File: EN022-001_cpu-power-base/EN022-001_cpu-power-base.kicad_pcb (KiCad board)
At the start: 2 copper layers, 100 x 100 mm, 31 parts, among them J1 MEGA BOTTOM, J10 GBA_Slot, J3 CART SLOT TOP ROW, J4 CART SLOT FRONT ROW, J6 5V USB, J7 Conn_01x07, J8 EXP2, J9 EXP1, M2_1 Screw_Terminal_01x01, M2_2 Screw_Terminal_01x01, M2_3 Screw_Terminal_01x01, M2_4 Screw_Terminal_01x01, M2_5 Screw_Terminal_01x01, M2_6 Screw_Terminal_01x01, M2_7 Screw_Terminal_01x01, M2_8 Screw_Terminal_01x01, M2_9 Screw_Terminal_01x01, SW1 VOLTAGE, SW2 POWER, U1 TPS2113PW, U2 DS3231MZ

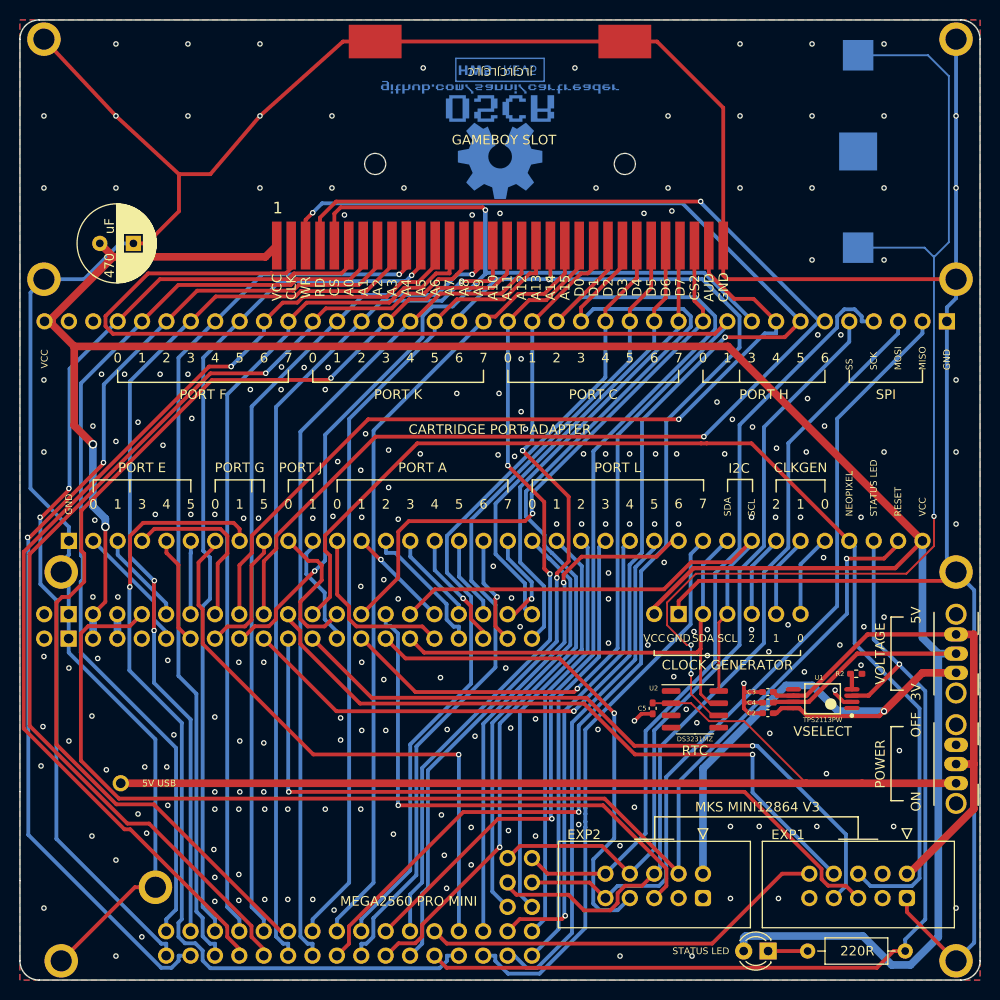
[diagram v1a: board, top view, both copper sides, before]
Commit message: mountin holes position
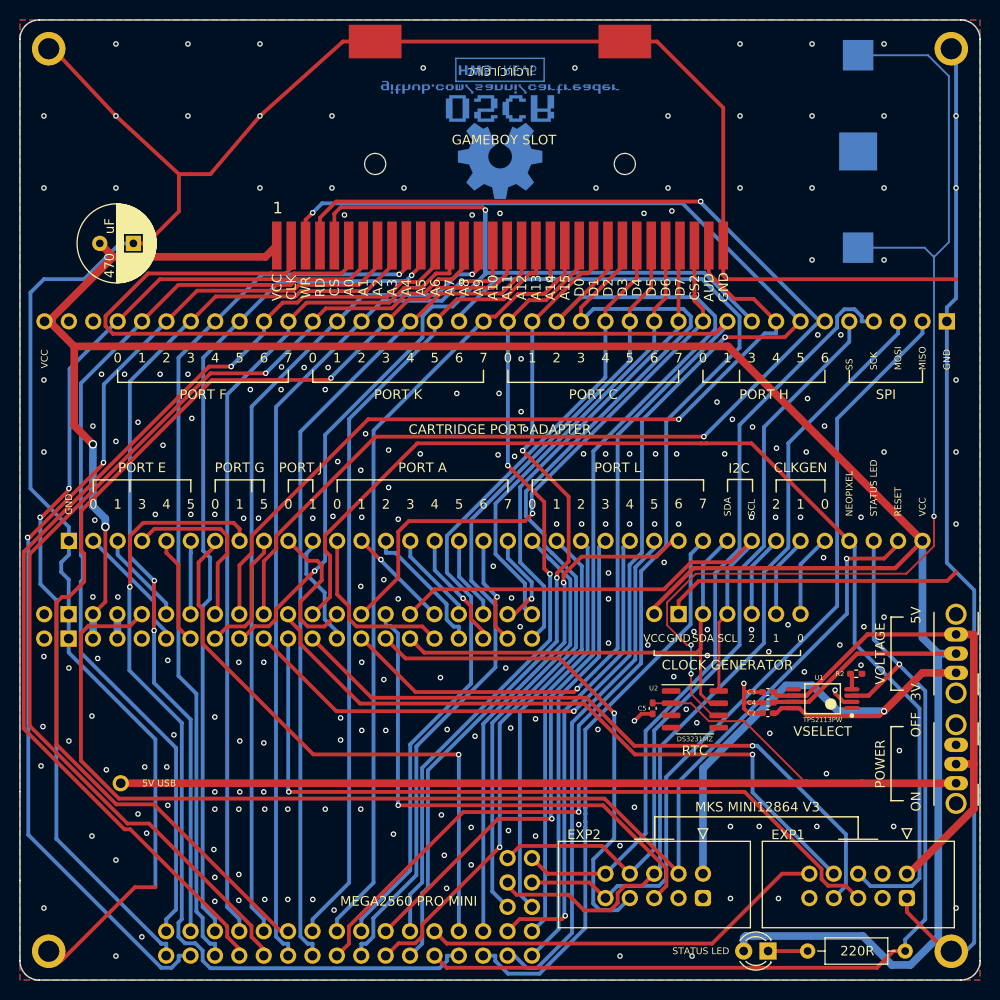
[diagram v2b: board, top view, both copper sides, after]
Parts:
- removed M2_5, M2_6, M2_7, M2_8, M2_9: Screw_Terminal_01x01, MountingHole:MountingHole_2.2mm_M2_ISO7380_Pad
- moved M2_3 117.6 mm to (103.0, 147.0)
- moved M2_4 39.5 mm to (197.0, 147.0)
- moved M2_1 1.12 mm to (103.0, 53.0)
- moved M2_2 1.12 mm to (197.0, 53.0)

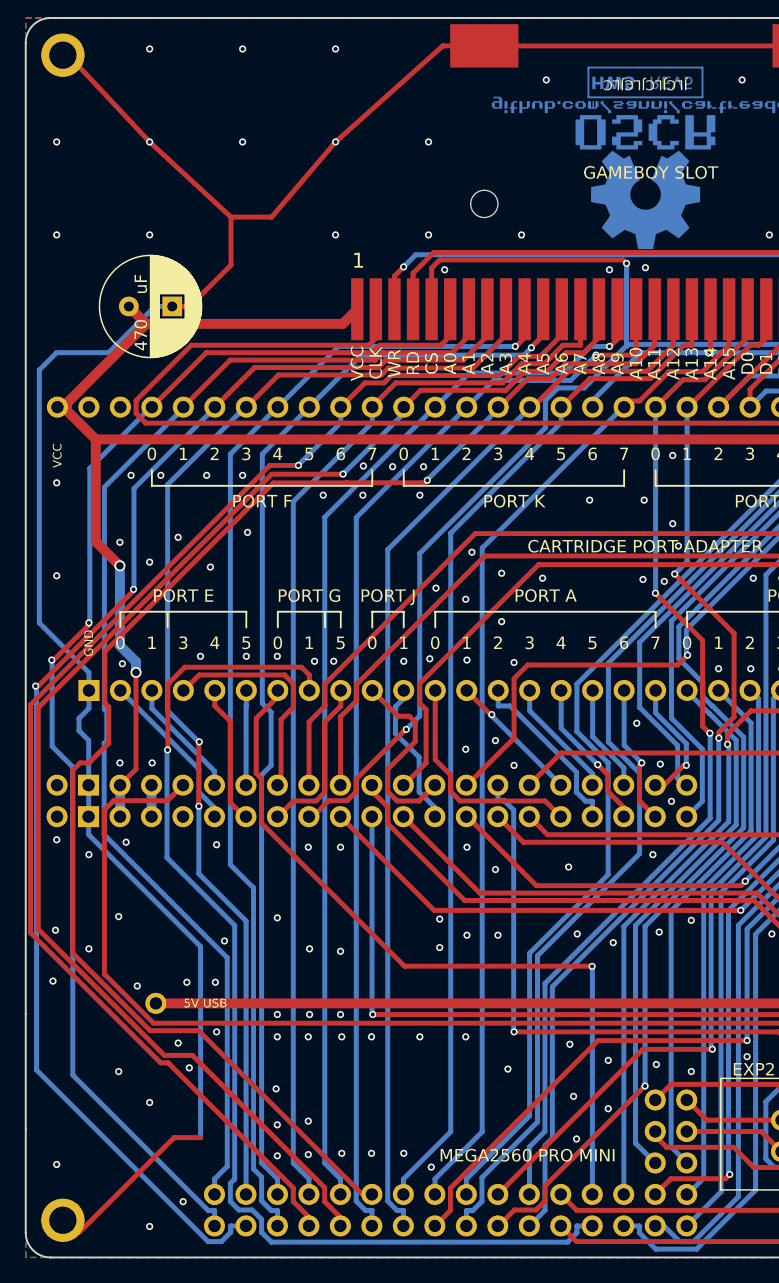
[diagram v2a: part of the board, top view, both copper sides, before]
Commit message: Removed atmega board connector
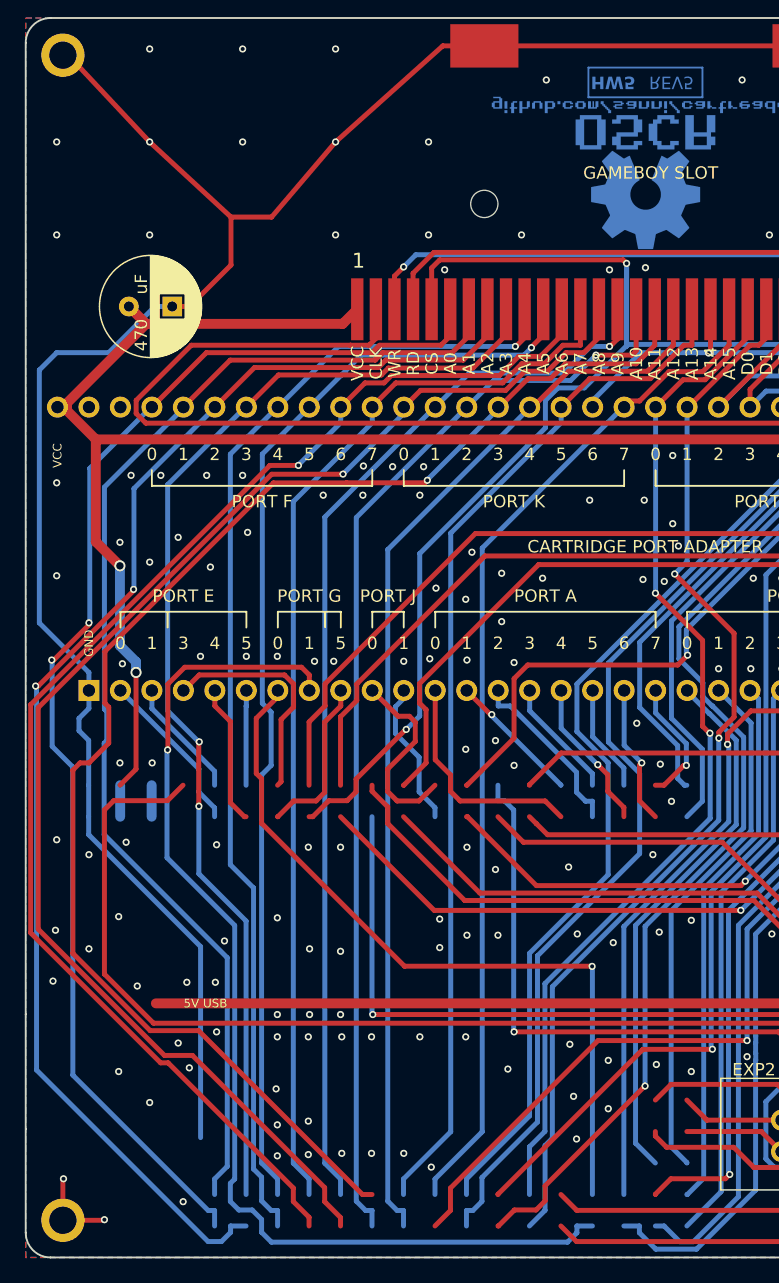
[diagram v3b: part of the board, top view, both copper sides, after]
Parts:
- removed J1: MEGA BOTTOM, !OSCR:MEGA2560_PRO_MINI
- removed J6: 5V USB, Connector_PinHeader_2.54mm:PinHeader_1x01_P2.54mm_Vertical
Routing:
- net GND: track 382.8 -> 376.5 mm
- net +3.3VA: track 2.54 -> 0.00 mm
- net (no net): track 0.00 -> 2.54 mm
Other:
- board text removed: "JLCJLCJLCJLC"

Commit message: updateted GBA slot
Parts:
- added U3: CH32V307VCT6, Package_QFP:LQFP-100_14x14mm_P0.5mm, F.Cu at (147.3, 122.8)
- added U7: AMS1117-3.3, Package_TO_SOT_SMD:SOT-223-3_TabPin2, F.Cu at (108.6, 139.3)
- J10: footprint !sanni:GBA-SLOT-B -> !OSCR:GBA_Slot
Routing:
- net A12: track 88.2 -> 86.9 mm, vias 0 -> 1
- net GND: vias 215 -> 212
- net D41: vias 1 -> 2
- net D39: vias 0 -> 1
- net D38: vias 1 -> 2
- net D35: vias 1 -> 2
- net D34: vias 1 -> 2
- net D33: vias 0 -> 1
- net D32: vias 0 -> 1
- net A9: vias 1 -> 2
- net A8: vias 1 -> 2
- net A7: vias 0 -> 1
- net A5: vias 1 -> 2
- net A4: vias 1 -> 2
- net A3: vias 2 -> 3
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
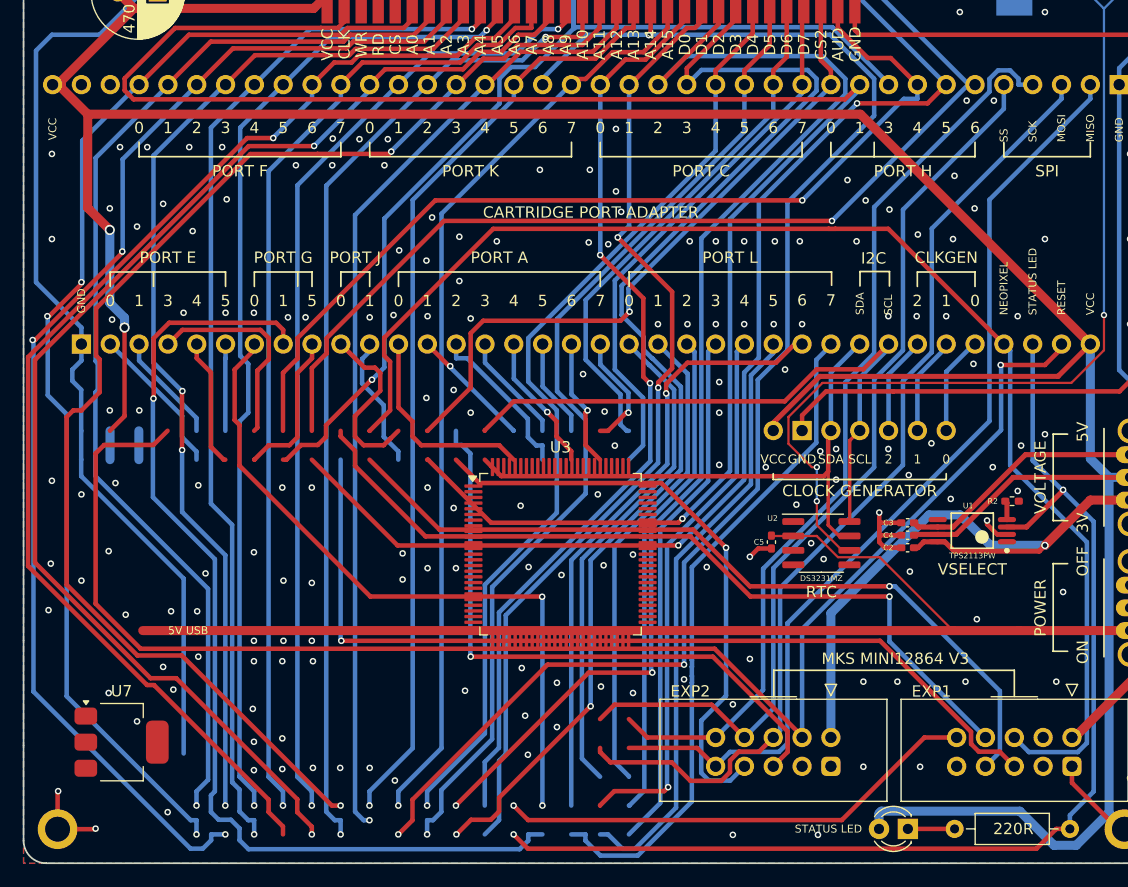
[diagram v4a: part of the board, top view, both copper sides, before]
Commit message: pcb traces cleanup
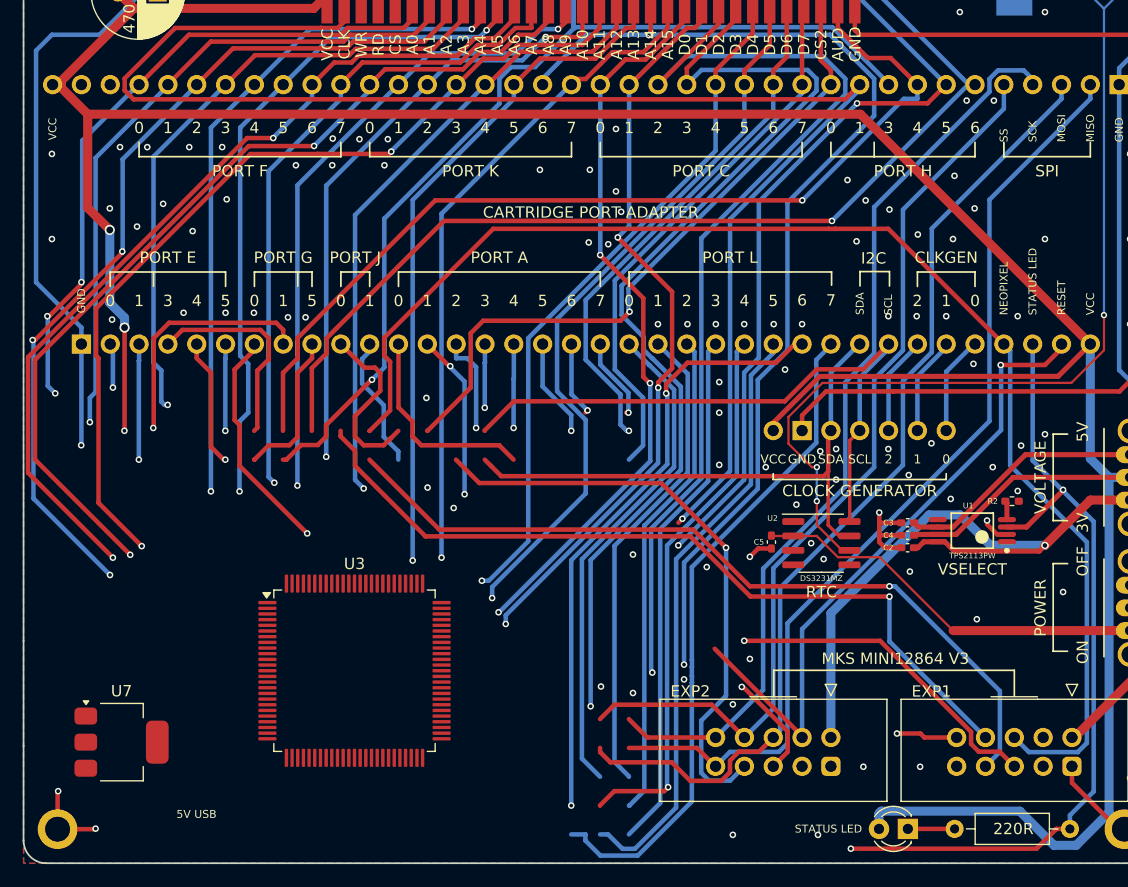
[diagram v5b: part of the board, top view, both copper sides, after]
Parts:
- moved U3 20.9 mm to (129.2, 133.0)
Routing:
- net RESET: track 134.1 -> 57.5 mm
- net VBUS: track 106.5 -> 35.1 mm
- net D40: track 89.7 -> 21.4 mm
- net D10: track 80.5 -> 29.0 mm
- net D19: track 55.0 -> 9.26 mm
- net A0: track 103.9 -> 59.6 mm
- net D41: track 61.5 -> 20.1 mm, vias 2 -> 1
- net A1: track 98.4 -> 60.2 mm
- net A3: track 94.3 -> 57.0 mm, vias 3 -> 1
- net D39: track 42.6 -> 5.40 mm
- net A11: track 115.9 -> 80.2 mm
- net D8: track 149.5 -> 114.1 mm
- net A10: track 89.5 -> 55.4 mm
- net A8: track 113.4 -> 80.8 mm
- net A14: track 127.6 -> 95.1 mm, vias 3 -> 2
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
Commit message: first cimplete  version of CPU POWER BASE
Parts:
- removed BT1: CR1616, !OSCR:CR1616
- removed C3: 0.1u, Capacitor_SMD:C_0402_1005Metric_Pad0.74x0.62mm_HandSolder
- removed J7: Conn_01x07, !OSCR:Clock_Generator_Header
- removed J8: EXP2, !OSCR:LCD_Header
- removed J9: EXP1, !OSCR:LCD_Header
- removed SW1: VOLTAGE, !OSCR:Power_Switch
- removed U7: AMS1117-3.3, Package_TO_SOT_SMD:SOT-223-3_TabPin2
- added C10: 10uF, Capacitor_SMD:C_1206_3216Metric_Pad1.33x1.80mm_HandSolder, F.Cu at (161.9, 130.7)
- added C11: 10uF, Capacitor_SMD:C_1206_3216Metric_Pad1.33x1.80mm_HandSolder, F.Cu at (182.3, 110.5)
- added C12: 10uF, Capacitor_SMD:C_1206_3216Metric_Pad1.33x1.80mm_HandSolder, F.Cu at (193.2, 119.7)
- added C13: 10uF, Capacitor_SMD:C_1206_3216Metric_Pad1.33x1.80mm_HandSolder, F.Cu at (180.0, 119.7)
- added C14: 100nF, Capacitor_SMD:C_0805_2012Metric_Pad1.18x1.45mm_HandSolder, F.Cu at (187.1, 134.4)
- added C200: 100nF, Capacitor_SMD:C_0805_2012Metric_Pad1.18x1.45mm_HandSolder, F.Cu at (122.9, 120.3)
- added C201: 100nF, Capacitor_SMD:C_0805_2012Metric_Pad1.18x1.45mm_HandSolder, F.Cu at (143.7, 125.5)
- added C202: 100nF, Capacitor_SMD:C_0805_2012Metric_Pad1.18x1.45mm_HandSolder, F.Cu at (137.6, 138.8)
- added C203: 100nF, Capacitor_SMD:C_0805_2012Metric_Pad1.18x1.45mm_HandSolder, F.Cu at (118.8, 136.2)
- added C204: 100nF, Capacitor_SMD:C_0805_2012Metric_Pad1.18x1.45mm_HandSolder, F.Cu at (143.7, 131.6)
- added C300: 100nF, Capacitor_SMD:C_0805_2012Metric_Pad1.18x1.45mm_HandSolder, F.Cu at (129.0, 85.2)
- added C301: 100nF, Capacitor_SMD:C_0805_2012Metric_Pad1.18x1.45mm_HandSolder, F.Cu at (151.8, 85.2)
- added C302: 100nF, Capacitor_SMD:C_0805_2012Metric_Pad1.18x1.45mm_HandSolder, F.Cu at (174.7, 85.2)
- added C8: 10uF, Capacitor_SMD:C_1206_3216Metric_Pad1.33x1.80mm_HandSolder, F.Cu at (161.9, 138.9)
- added C9: 470uF, Capacitor_SMD:CP_Elec_6.3x7.7, F.Cu at (195.5, 111.3)
- added D2: 600mV@200mA, Diode_SMD:D_SOD-123F, F.Cu at (184.6, 119.9)
- added D7: 600mV@200mA, Diode_SMD:D_SOD-123F, F.Cu at (178.5, 134.9)
- added J2: USB_C_Receptacle_USB2.0_16P, Connector_USB:USB_C_Receptacle_GCT_USB4105-xx-A_16P_TopMnt_Horizontal, F.Cu at (133.0, 146.4)
- added J5: Conn_02x05_Odd_Even, Connector_PinSocket_2.54mm:PinSocket_2x05_P2.54mm_Horizontal, F.Cu at (111.3, 131.1)
- added J6: Conn_01x04, Connector_PinHeader_2.54mm:PinHeader_1x04_P2.54mm_Vertical, F.Cu at (115.0, 117.2)
- added JP1: Jumper_2_Bridged, Connector_PinHeader_2.54mm:PinHeader_1x02_P2.54mm_Vertical, F.Cu at (141.4, 137.3)
- added JP2: Jumper_2_Bridged, Connector_PinHeader_2.54mm:PinHeader_1x02_P2.54mm_Vertical, F.Cu at (123.4, 114.2)
- added LD1: LED_Filled, LED_SMD:LED_0805_2012Metric_Pad1.15x1.40mm_HandSolder, F.Cu at (176.2, 146.4)
- added LD2: LED_Filled, LED_SMD:LED_0805_2012Metric_Pad1.15x1.40mm_HandSolder, F.Cu at (191.4, 146.4)
- added LD3: LED_Filled, LED_SMD:LED_0805_2012Metric_Pad1.15x1.40mm_HandSolder, F.Cu at (185.0, 146.5)
- added Q3: KY6802, Package_TO_SOT_SMD:SOT-23-6_Handsoldering, F.Cu at (192.7, 127.8)
- added Q4: AO3401, Package_TO_SOT_SMD:SOT-23, F.Cu at (189.3, 112.2)
- added Q5: AO3401, Package_TO_SOT_SMD:SOT-23, F.Cu at (176.5, 112.3)
- added Q6: KY6802, Package_TO_SOT_SMD:SOT-23-6_Handsoldering, F.Cu at (170.1, 127.9)
- added Q7: AO3401, Package_TO_SOT_SMD:SOT-23, F.Cu at (176.4, 108.0)
- added Q9: AO3401, Package_TO_SOT_SMD:SOT-23, F.Cu at (189.3, 108.2)
- added R10: 10k, Resistor_SMD:R_0805_2012Metric_Pad1.20x1.40mm_HandSolder, F.Cu at (130.7, 116.0)
- added R11: 1k, Resistor_SMD:R_0805_2012Metric_Pad1.20x1.40mm_HandSolder, F.Cu at (184.8, 134.4)
- added R12: 0R, Resistor_SMD:R_0805_2012Metric_Pad1.20x1.40mm_HandSolder, F.Cu at (187.9, 96.7)
- added R14: 1k, Resistor_SMD:R_0805_2012Metric_Pad1.20x1.40mm_HandSolder, F.Cu at (185.0, 142.4)
- added R15: 1k, Resistor_SMD:R_0805_2012Metric_Pad1.20x1.40mm_HandSolder, F.Cu at (175.4, 120.3)
- added R16: 1k, Resistor_SMD:R_0805_2012Metric_Pad1.20x1.40mm_HandSolder, F.Cu at (196.3, 127.6)
- added R19: 10k, Resistor_SMD:R_0805_2012Metric_Pad1.20x1.40mm_HandSolder, F.Cu at (173.9, 134.4)
- added R20: 10k, Resistor_SMD:R_0805_2012Metric_Pad1.20x1.40mm_HandSolder, F.Cu at (167.0, 141.9)
- added R22: 10k, Resistor_SMD:R_0805_2012Metric_Pad1.20x1.40mm_HandSolder, F.Cu at (189.4, 115.7)
- added R24: 1k, Resistor_SMD:R_0805_2012Metric_Pad1.20x1.40mm_HandSolder, F.Cu at (176.2, 127.9)
- added R25: 10k, Resistor_SMD:R_0805_2012Metric_Pad1.20x1.40mm_HandSolder, F.Cu at (176.4, 115.7)
- added R28: 10k, Resistor_SMD:R_0805_2012Metric_Pad1.20x1.40mm_HandSolder, F.Cu at (195.3, 120.3)
- added R29: 10k, Resistor_SMD:R_0805_2012Metric_Pad1.20x1.40mm_HandSolder, F.Cu at (182.3, 120.3)
- added R30: 1k, Resistor_SMD:R_0805_2012Metric_Pad1.20x1.40mm_HandSolder, F.Cu at (176.2, 142.4)
- added R31: 1M, Resistor_SMD:R_0805_2012Metric_Pad1.20x1.40mm_HandSolder, F.Cu at (176.2, 134.4)
- added R36: 1k, Resistor_SMD:R_0805_2012Metric_Pad1.20x1.40mm_HandSolder, F.Cu at (169.0, 141.9)
- added R4: 10k, Resistor_SMD:R_0805_2012Metric_Pad1.20x1.40mm_HandSolder, F.Cu at (153.6, 140.3)
- added R5: 0R, Resistor_SMD:R_0805_2012Metric_Pad1.20x1.40mm_HandSolder, F.Cu at (118.8, 133.6)
- added R6: 10k, Resistor_SMD:R_0805_2012Metric_Pad1.20x1.40mm_HandSolder, F.Cu at (144.8, 138.8)
- added R7: 0R, Resistor_SMD:R_0805_2012Metric_Pad1.20x1.40mm_HandSolder, F.Cu at (118.8, 131.1)
- added R8: 1k, Resistor_SMD:R_0805_2012Metric_Pad1.20x1.40mm_HandSolder, F.Cu at (111.2, 112.2)
- added R9: 1k, Resistor_SMD:R_0805_2012Metric_Pad1.20x1.40mm_HandSolder, F.Cu at (111.2, 109.9)
- added SW3: TC-6615-7-260G, Button_Switch_THT:SW_Tactile_SPST_Angled_PTS645Vx58-2LFS, F.Cu at (155.6, 147.5)
- added U100: CH32V30xRxTx, Package_QFP:LQFP-64_10x10mm_P0.5mm, F.Cu at (132.5, 127.8)
- added U300: MCP23S17_SS, Package_SO:SSOP-28_5.3x10.2mm_P0.65mm, F.Cu at (127.9, 92.0)
- added U301: MCP23S17_SS, Package_SO:SSOP-28_5.3x10.2mm_P0.65mm, F.Cu at (150.8, 92.0)
- added U302: MCP23S17_SS, Package_SO:SSOP-28_5.3x10.2mm_P0.65mm, F.Cu at (173.7, 92.0)
- added U4: W25Q32JVSS, Package_SO:SOIC-8_5.3x5.3mm_P1.27mm, F.Cu at (139.6, 111.9)
- added Y1: 8MHz 10pF, Crystal:Crystal_SMD_3225-4Pin_3.2x2.5mm_HandSoldering, F.Cu at (150.7, 129.5)
- C1: value 470u -> 12pF; footprint Capacitor_THT:CP_Radial_D8.0mm_P3.50mm -> Capacitor_SMD:C_0603_1608Metric_Pad1.08x0.95mm_HandSolder
- C2: value 0.1u -> 10uF; footprint Capacitor_SMD:C_0402_1005Metric_Pad0.74x0.62mm_HandSolder -> Capacitor_SMD:C_1206_3216Metric_Pad1.33x1.80mm_HandSolder
- C4: value 10u -> 10nF; footprint Capacitor_SMD:C_0402_1005Metric_Pad0.74x0.62mm_HandSolder -> Capacitor_SMD:C_0805_2012Metric_Pad1.18x1.45mm_HandSolder
- C5: value 0.1u -> 12pF; footprint Capacitor_SMD:C_0402_1005Metric_Pad0.74x0.62mm_HandSolder -> Capacitor_SMD:C_0603_1608Metric_Pad1.08x0.95mm_HandSolder
- D1: value LED -> 600mV@200mA; footprint LED_THT:LED_D3.0mm -> Diode_SMD:D_SOD-123F
- R1: value 220R -> 1k; footprint Resistor_THT:R_Axial_DIN0207_L6.3mm_D2.5mm_P10.16mm_Horizontal -> Resistor_SMD:R_0805_2012Metric_Pad1.20x1.40mm_HandSolder
- R2: value 560R -> 1k; footprint Resistor_SMD:R_0402_1005Metric_Pad0.72x0.64mm_HandSolder -> Resistor_SMD:R_0805_2012Metric_Pad1.20x1.40mm_HandSolder
- SW2: value POWER -> SK12D07VG3; footprint !OSCR:Power_Switch -> Button_Switch_THT:SW_Slide_SPDT_Angled_CK_OS102011MA1Q
- U1: value TPS2113PW -> 74HC132D,653; footprint Personal:Texas_Instruments-TPS2113PW-Level_A -> Package_SO:SOIC-14_3.9x8.7mm_P1.27mm
- U2: value DS3231MZ -> ETA5060V330S8F; footprint Package_SO:SOIC-8_3.9x4.9mm_P1.27mm -> Package_TO_SOT_SMD:SOT-89-5
- U3: value CH32V307VCT6 -> SGM4568YTS20G/TR; footprint Package_QFP:LQFP-100_14x14mm_P0.5mm -> Package_SO:TSSOP-20_4.4x6.5mm_P0.65mm
- moved C1 67.3 mm to (150.4, 125.8), turned to 180 degrees
- moved U3 43.1 mm to (108.4, 95.3)
- moved SW2 37.1 mm to (165.0, 147.5), turned to 0 degrees
- moved D1 33.4 mm to (197.5, 119.9), turned to -90 degrees
- moved R1 27.4 mm to (188.4, 120.3), turned to -90 degrees
- moved R2 24.7 mm to (191.4, 142.4), turned to -90 degrees
- moved C5 19.2 mm to (150.5, 133.2), turned to 180 degrees
- moved U2 15.6 mm to (161.7, 134.8)
- moved C2 13.1 mm to (181.0, 134.9), turned to -90 degrees
- moved C4 7.92 mm to (173.9, 127.9), turned to -90 degrees
- moved U1 7.24 mm to (182.3, 127.8), turned to -90 degrees
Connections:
- C1 pad 1: VCC -> GND
- C1 pad 2: GND -> Net-(U100-OSC_OUT)
- C2 pad 1: GND -> Net-(D7-K)
- C2 pad 2: +3V3 -> GND
- C4 pad 1: VCC -> Net-(Q6B-D)
- C5 pad 1: VBUS -> Net-(U100-OSC_IN)
- D1 pad 2: VCC -> Net-(D1-A)
- J10 pad 1: VCC -> VDD-CART
- J3 pad 1: VCC -> VDD-CART
- J4 pad 36: VCC -> VDD-CART
- M2_1 pad 1: GND -> unconnected-(M2_1-Pin_1-Pad1)
- M2_2 pad 1: GND -> unconnected-(M2_2-Pin_1-Pad1)
- M2_3 pad 1: GND -> unconnected-(M2_3-Pin_1-Pad1)
- M2_4 pad 1: GND -> unconnected-(M2_4-Pin_1-Pad1)
- R1 pad 1: Net-(D1-K) -> Net-(Q4-G)
- R1 pad 2: D38 -> Net-(R1-Pad2)
- R2 pad 1: GND -> Net-(Q4-D)
- R2 pad 2: Net-(U1-ILIM) -> Net-(LD2-A)
- SW2 pad 1: VBUS -> GND
- SW2 pad 2: +5V -> /POWER1/POWON
- SW2 pad 3: unconnected-(SW2-C-Pad3) -> Net-(SW2-C)
- U1 pad 1: unconnected-(U1-STAT-Pad1) -> Net-(Q3B-D)
- U1 pad 2: GND -> Net-(D1-A)
- U1 pad 3: D38 -> Net-(R1-Pad2)
- U1 pad 4: Net-(U1-ILIM) -> Net-(Q3B-D)
- U1 pad 5: GND -> Net-(D2-A)
- U1 pad 6: +5V -> Net-(R15-Pad2)
- U1 pad 7: VCC -> GND
- U1 pad 8: +3V3 -> Net-(Q6A-G)
- U2 pad 2: VBUS -> GND
- U2 pad 3: unconnected-(U2-~{INT}/SQW-Pad3) -> /POWER1/POWON
- U2 pad 4: unconnected-(U2-~{RST}-Pad4) -> 5V-USB
- U2 pad 5: GND -> +3V3
- U3 pad 1: unconnected-(U3-PE2-Pad1) -> /Base Connector/IOEXP_RST
- U3 pad 10: unconnected-(U3-VSS-Pad10) -> +3V3
- U3 pad 11: unconnected-(U3-VDD-Pad11) -> GND
- U3 pad 12: unconnected-(U3-OSC_IN-Pad12) -> D15
- U3 pad 13: unconnected-(U3-OSC_OUT-Pad13) -> D14
- U3 pad 14: unconnected-(U3-NRST-Pad14) -> D5
- U3 pad 15: unconnected-(U3-PC0/ADC10-Pad15) -> Net-(U3-B5)
- U3 pad 16: unconnected-(U3-PC1/ADC11-Pad16) -> /Base Connector/IOEXP_SDO_
- U3 pad 17: unconnected-(U3-PC2/ADC12-Pad17) -> /Base Connector/IOEXP_SDI_
- U3 pad 18: unconnected-(U3-PC3/ADC13-Pad18) -> /Base Connector/IOEXP_SCK_
- U3 pad 19: unconnected-(U3-VSSA-Pad19) -> VDD-CART
- U3 pad 2: unconnected-(U3-PE3-Pad2) -> +3V3
- U3 pad 20: unconnected-(U3-VREF--Pad20) -> /Base Connector/IOEXP_RSTn_
- U3 pad 3: unconnected-(U3-PE4-Pad3) -> /Base Connector/IOEXP_SCK
- U3 pad 4: unconnected-(U3-PE5-Pad4) -> /Base Connector/IOEXP_SDI
- U3 pad 5: unconnected-(U3-PE6-Pad5) -> /Base Connector/IOEXP_SDO
- U3 pad 6: unconnected-(U3-VBAT-Pad6) -> /Base Connector/IOEXP_D16
- U3 pad 7: unconnected-(U3-PC13/TAMPER-RTC-Pad7) -> /Base Connector/IOEXP_D05
- U3 pad 8: unconnected-(U3-PC14/OSC32IN-Pad8) -> /Base Connector/IOEXP_D14
- U3 pad 9: unconnected-(U3-PC15/OSC32OUT-Pad9) -> /Base Connector/IOEXP_D15
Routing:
- net VCC: track 279.8 -> 0.00 mm, vias 3 -> 0
- net GND: track 345.0 -> 135.6 mm, vias 134 -> 100
- net D13: track 117.4 -> 0.00 mm
- net +BATT: track 113.2 -> 0.00 mm, vias 3 -> 0
- net /Base Connector/IOEXP_RSTn_: track 0.00 -> 98.0 mm, vias 0 -> 4
- net /Base Connector/IOEXP_SCK_: track 0.00 -> 90.0 mm, vias 0 -> 4
- net /Base Connector/IOEXP_SDI_: track 0.00 -> 88.6 mm, vias 0 -> 4
- net /Base Connector/IOEXP_SDO_: track 0.00 -> 87.4 mm, vias 0 -> 4
- net D51: track 86.9 -> 0.00 mm
- net Net-(U3-B5): track 0.00 -> 86.1 mm, vias 0 -> 2
- net D50: track 84.6 -> 0.00 mm
- net VDD-CART: track 0.00 -> 81.9 mm, vias 0 -> 8
- net D53: track 81.4 -> 0.00 mm
- net D52: track 81.2 -> 0.00 mm
- net D38: track 72.2 -> 0.00 mm, vias 2 -> 0
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- added copper zone on In2.Cu, net +3V3
- added copper zone on In2.Cu, net 5V-USB
- added copper zone on In1.Cu, net GND
- added copper zone on In2.Cu, net VDD-CART
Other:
- outline, holes or cut-outs redrawn
- copper layers 2 -> 4
- board text added: "BOOT1"
- board text removed: "3V3"
- board text removed: "3V3 5V"
- board text removed: "D10"
- board text removed: "D11"
- board text removed: "D12"
- board text removed: "D18"
- board text removed: "D19"
- board text removed: "D39"
- board text removed: "EXP2"
- board text removed: "ON OFF"
- board text removed: "RTC BATTERY"
- board text removed: "VSELECT"
